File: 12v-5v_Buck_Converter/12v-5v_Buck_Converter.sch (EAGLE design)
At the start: 22 parts, among them J1 PJ-037A, U1 ZXMN3A01Z, U2 TERMINAL_BLOCK_2P, U3 TERMINAL_BLOCK_2P, U4 TERMINAL_BLOCK_2P, U5 TERMINAL_BLOCK_2P, U6 RT7258GSP

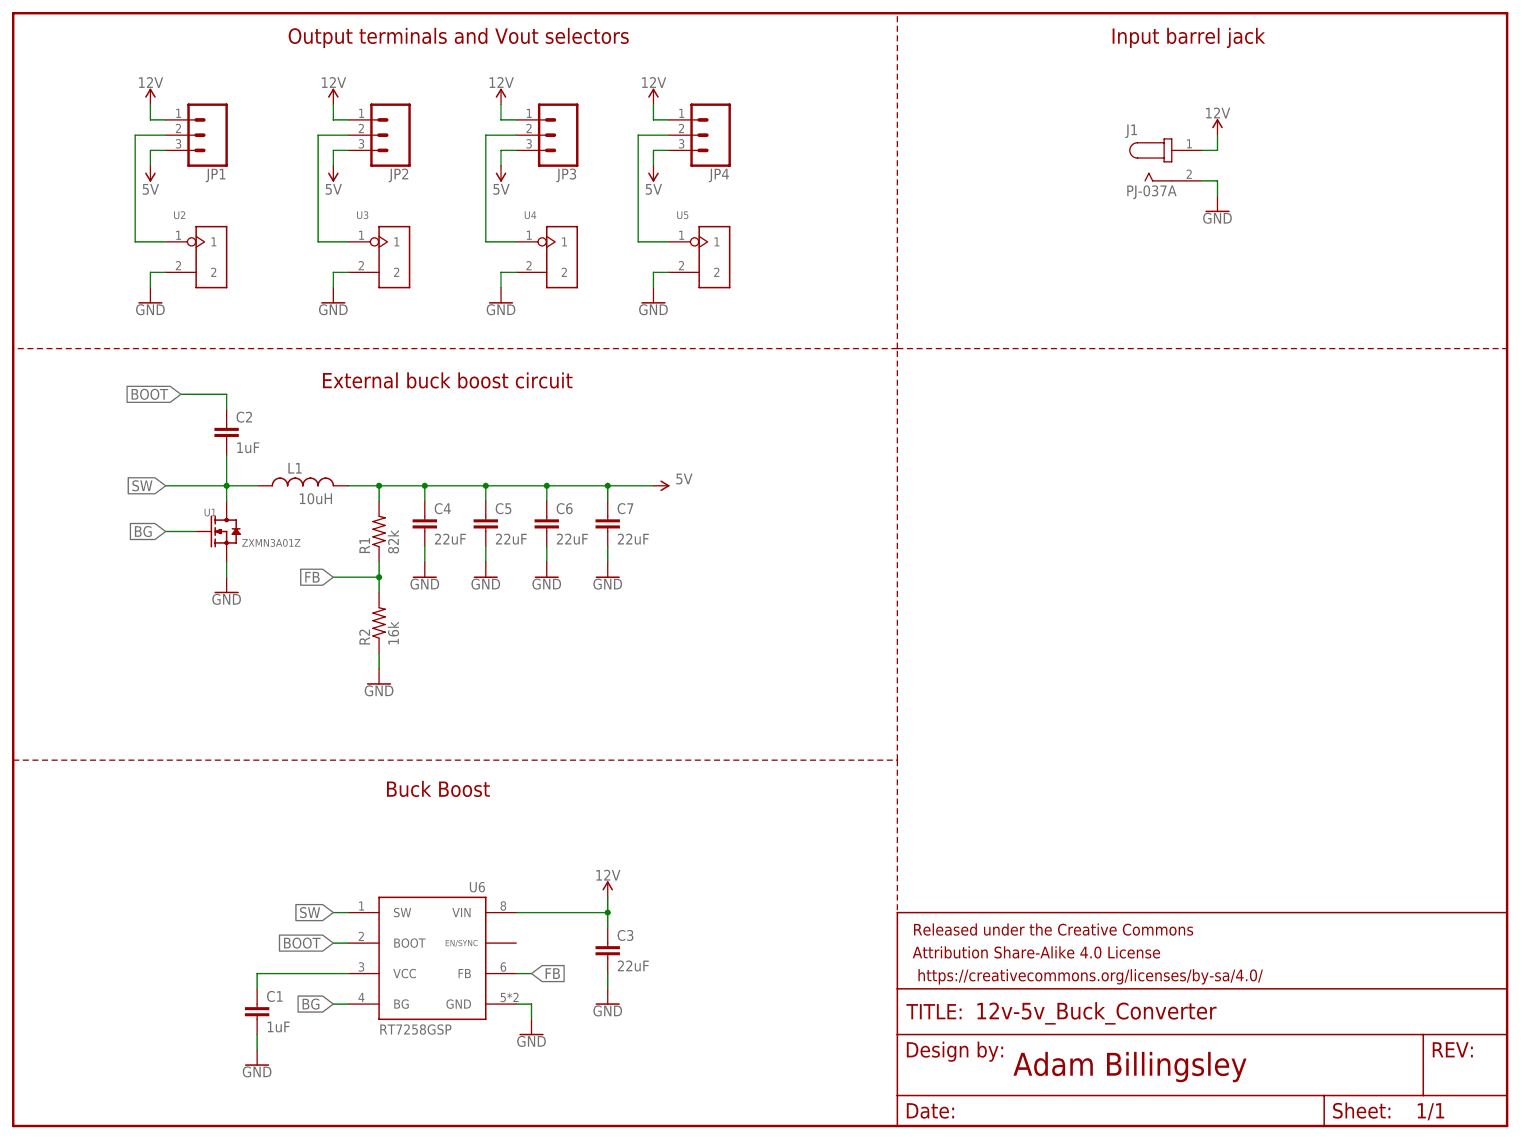
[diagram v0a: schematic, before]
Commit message: Redesign to fix incorrect specs
MOSFET needed to have a Vgs of 5V and all of the other passive components were adjusted to be more temperature/current compatible
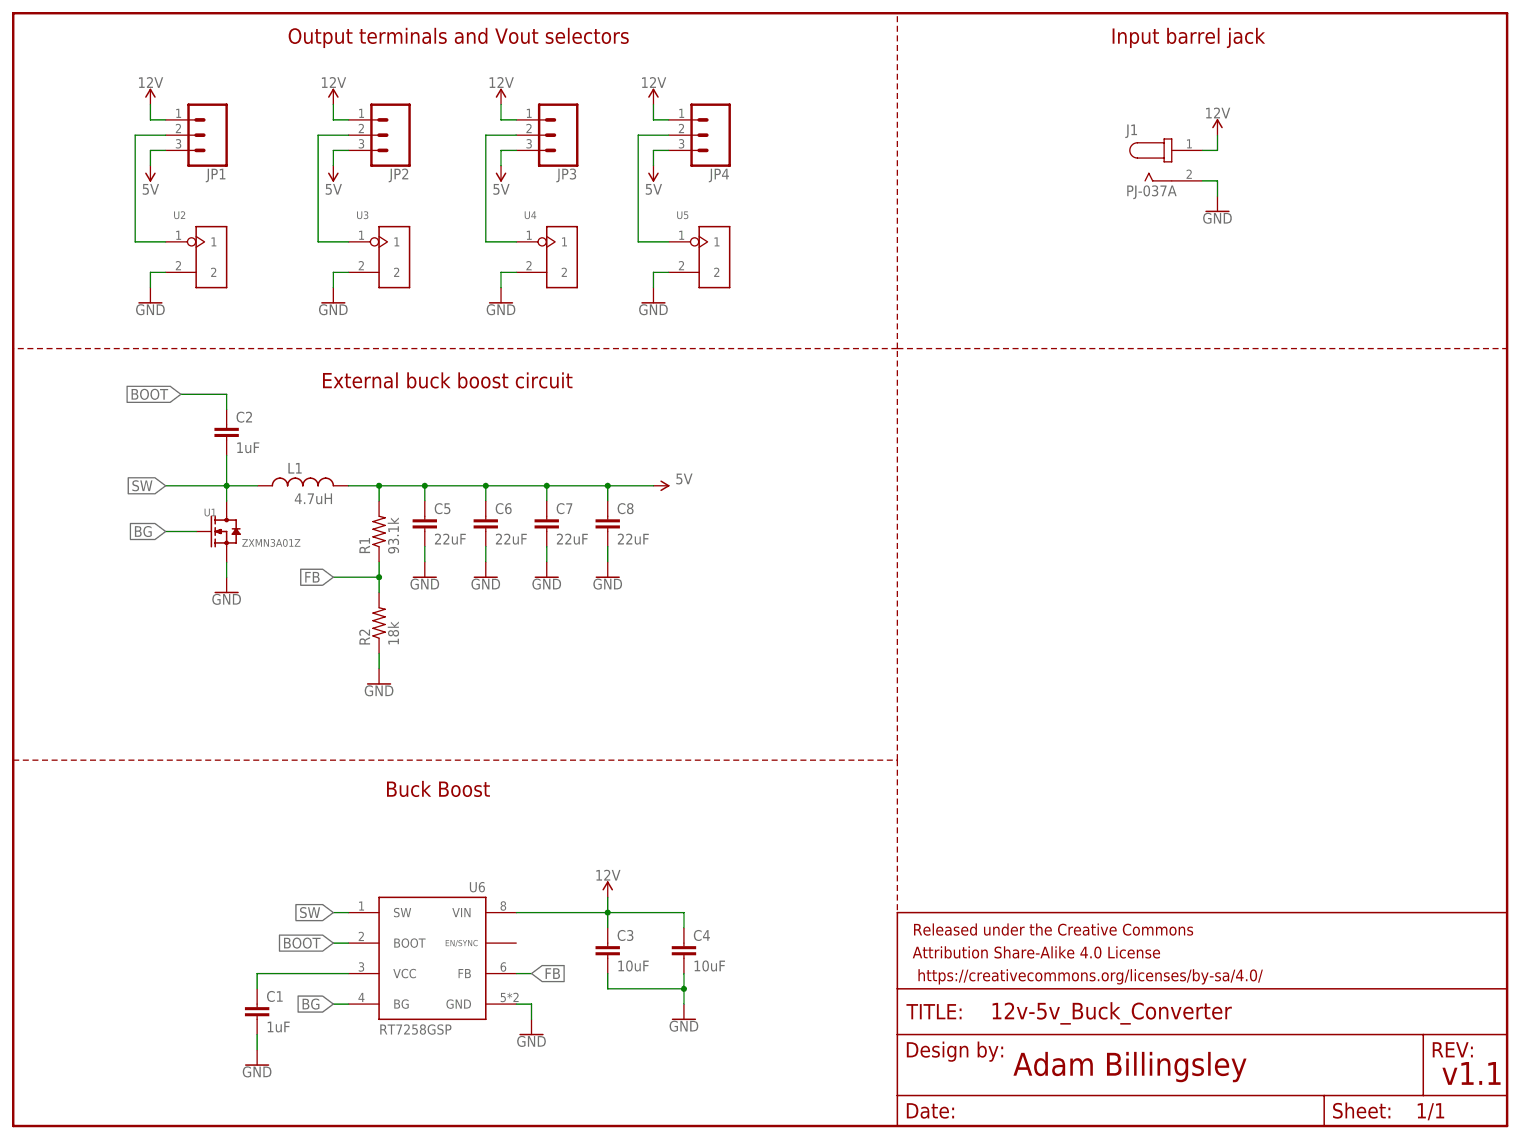
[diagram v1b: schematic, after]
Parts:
- added C8: 22uF, Adam's Parts (work):1210_CAPACITOR
- C1, C2: device Adam's Parts (work):0603_CAPACITOR -> Adam's Parts (work):1206_CAPACITOR
- C3, C4: value 22uF -> 10uF; device Adam's Parts (work):0805_CAPACITOR -> Adam's Parts (work):1206_CAPACITOR
- C5, C6, C7: device Adam's Parts (work):0805_CAPACITOR -> Adam's Parts (work):1210_CAPACITOR
- L1: value 10uH -> 4.7uH; device Adam's Parts (work):INDUCTOR_LSXND5050YAL100MMG -> Adam's Parts (work):INDUCTOR_7443330470
- R1: value 82k -> 93.1k; device Adam's Parts (work):0603_RESISTOR -> Adam's Parts (work):1206_RESISTOR
- R2: value 16k -> 18k
- U1: device Adam's Parts (work):MOSFET-N-ZXMN3A01Z -> Adam's Parts (work):MOSFET-N-SI7114DN
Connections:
- net 12V: now also C4.1
- net 5V: now also C8.1; no longer C4.1
- net GND: now also C8.2
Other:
- note added: "v1.1"
- moved on the sheet: C4, C5, C6, C7
